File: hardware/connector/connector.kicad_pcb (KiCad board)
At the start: 2 copper layers, 60 x 40 mm, 4 parts

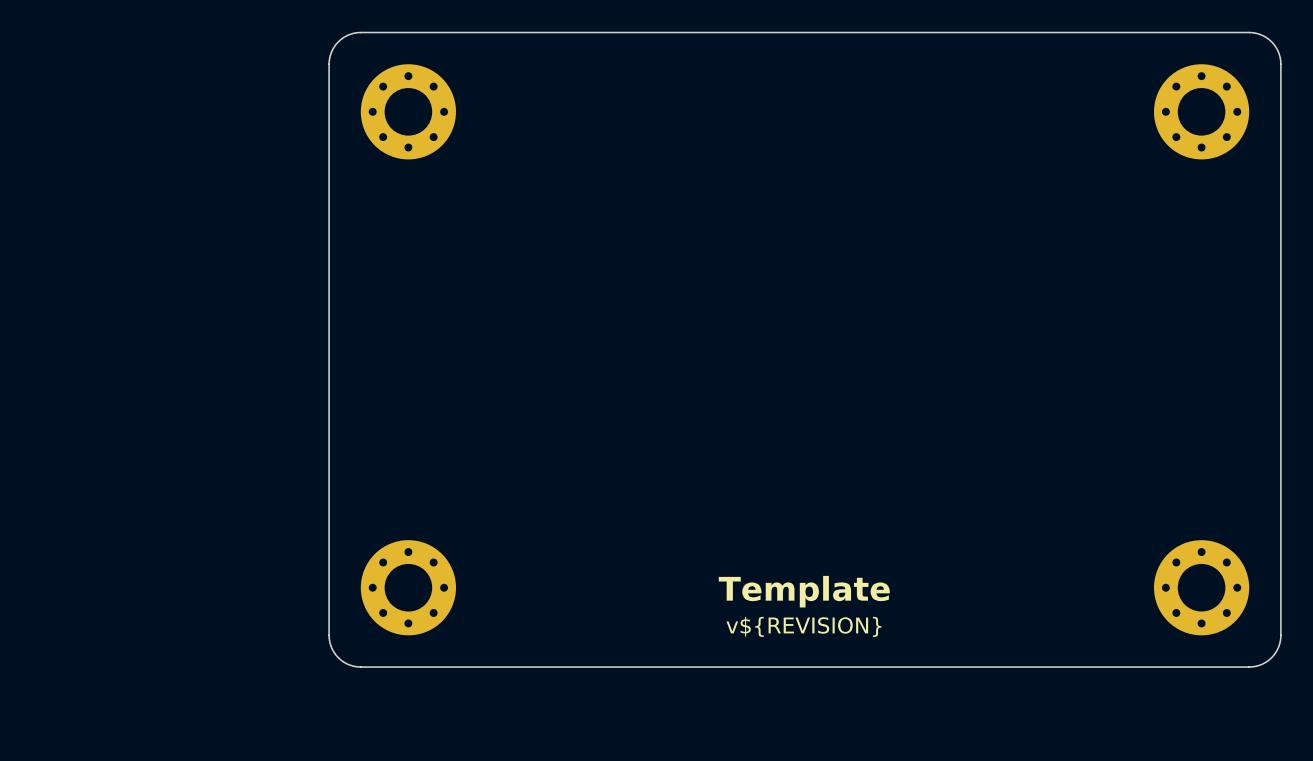
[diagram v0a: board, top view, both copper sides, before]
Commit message: Route PCB tracks
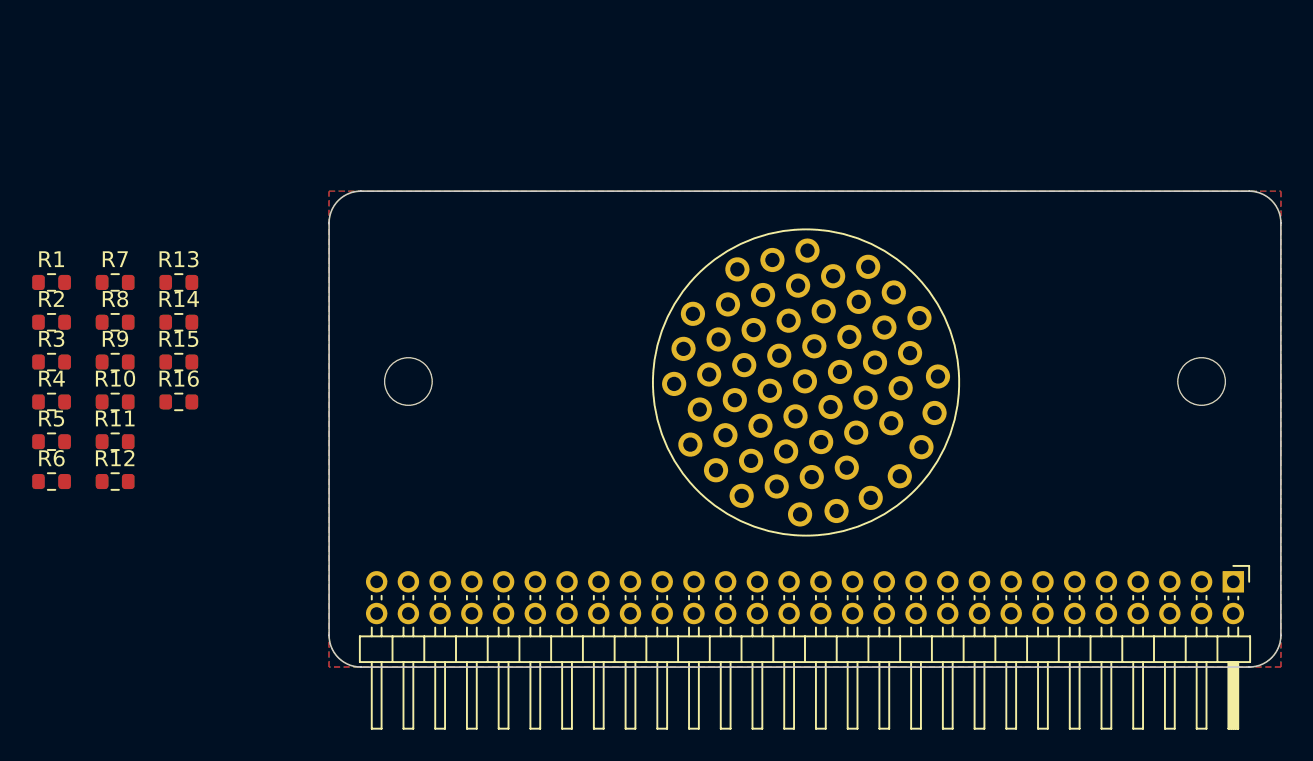
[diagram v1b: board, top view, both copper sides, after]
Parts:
- removed the REF** at (171.0, 81.0)
- removed the REF** at (121.0, 111.0)
- removed the REF** at (121.0, 81.0)
- removed the REF** at (171.0, 111.0)
- added J2: Autosport, Local_Library:AS022-55SN, B.Cu at (145.3, 98.6)
- added J3: Goldpin, Connector_PinHeader_2.00mm:PinHeader_2x28_P2.00mm_Horizontal, F.Cu at (173.0, 110.6)
- added R1: 0R, Resistor_SMD:R_0603_1608Metric, F.Cu at (98.5, 91.8)
- added R10: 0R, Resistor_SMD:R_0603_1608Metric, F.Cu at (102.5, 99.3)
- added R11: 0R, Resistor_SMD:R_0603_1608Metric, F.Cu at (102.5, 101.8)
- added R12: 0R, Resistor_SMD:R_0603_1608Metric, F.Cu at (102.5, 104.3)
- added R13: 0R, Resistor_SMD:R_0603_1608Metric, F.Cu at (106.5, 91.8)
- added R14: 0R, Resistor_SMD:R_0603_1608Metric, F.Cu at (106.5, 94.3)
- added R15: 0R, Resistor_SMD:R_0603_1608Metric, F.Cu at (106.5, 96.8)
- added R16: 0R, Resistor_SMD:R_0603_1608Metric, F.Cu at (106.5, 99.3)
- added R2: 0R, Resistor_SMD:R_0603_1608Metric, F.Cu at (98.5, 94.3)
- added R3: 0R, Resistor_SMD:R_0603_1608Metric, F.Cu at (98.5, 96.8)
- added R4: 0R, Resistor_SMD:R_0603_1608Metric, F.Cu at (98.5, 99.3)
- added R5: 0R, Resistor_SMD:R_0603_1608Metric, F.Cu at (98.5, 101.8)
- added R6: 0R, Resistor_SMD:R_0603_1608Metric, F.Cu at (98.5, 104.3)
- added R7: 0R, Resistor_SMD:R_0603_1608Metric, F.Cu at (102.5, 91.8)
- added R8: 0R, Resistor_SMD:R_0603_1608Metric, F.Cu at (102.5, 94.3)
- added R9: 0R, Resistor_SMD:R_0603_1608Metric, F.Cu at (102.5, 96.8)
- added REF**: MountingHole_3mm, MountingHole:MountingHole_3mm, F.Cu at (121.0, 98.0)
- added REF**: MountingHole_3mm, MountingHole:MountingHole_3mm, F.Cu at (171.0, 98.0)
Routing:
- added copper zone on B.Cu, net GND
- added copper zone on F.Cu, net GND
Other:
- board size 60 x 40 mm -> 60 x 30 mm
- board text removed: "Template"
- board text removed: "v${REVISION}"

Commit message: Route the tracks on the connector PCB
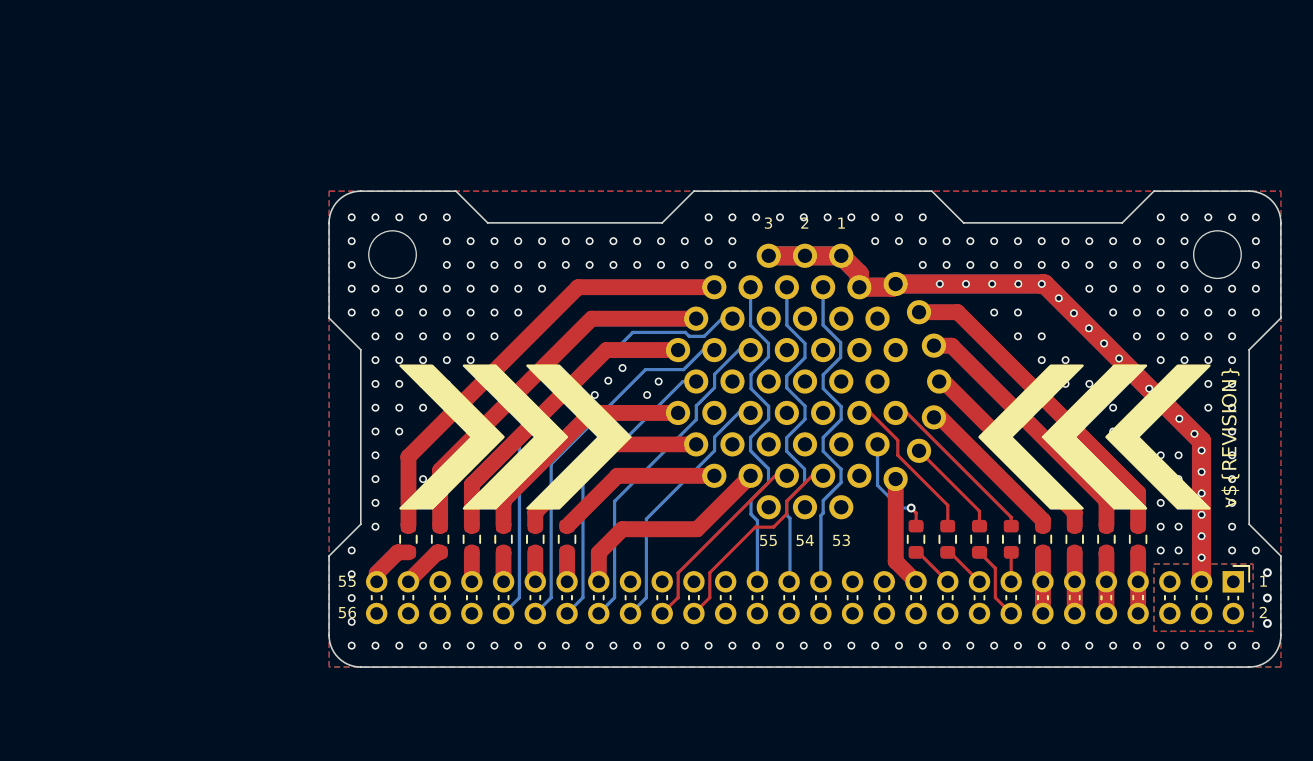
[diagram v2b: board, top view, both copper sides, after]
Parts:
- removed J3: Goldpin, Connector_PinHeader_2.00mm:PinHeader_2x28_P2.00mm_Horizontal
- removed R15, R16: 0R, Resistor_SMD:R_0603_1608Metric
- added J1: Conn_02x28_Top_Bottom, Local_Library:PinHeader_2x28_P2.00mm_Horizontal, F.Cu at (173.0, 110.6)
- J2: value Autosport -> D38999; footprint Local_Library:AS022-55SN -> Local_Library:DTS20W17-35SN
- moved R2 69.8 mm to (167.0, 107.9), turned to -90 degrees
- moved R4 67.1 mm to (165.0, 107.9), turned to -90 degrees
- moved R6 64.6 mm to (163.0, 107.9), turned to -90 degrees
- moved R7 60.7 mm to (161.0, 107.9), turned to -90 degrees
- moved R8 58.1 mm to (159.0, 107.9), turned to 90 degrees
- moved R11 54.8 mm to (157.0, 107.9), turned to 90 degrees
- moved R9 53.7 mm to (155.0, 107.9), turned to 90 degrees
- moved R12 50.6 mm to (153.0, 107.9), turned to 90 degrees
- moved R14 28.0 mm to (131.0, 107.9), turned to -90 degrees
- moved R1 27.7 mm to (121.0, 107.9), turned to 90 degrees
- moved R13 27.7 mm to (129.0, 107.9), turned to -90 degrees
- moved R5 27.2 mm to (125.0, 107.9), turned to 90 degrees
- moved R3 26.9 mm to (123.0, 107.9), turned to 90 degrees
- moved R10 26.0 mm to (127.0, 107.9), turned to -90 degrees
- moved REF** 8.06 mm to (120.0, 90.0)
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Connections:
- J2 pad 11: +5V_EXT -> SAFETY_IN_INV
- J2 pad 12: WATER_PRESSURE_IN1 -> SAFETY_IN_RES
- J2 pad 13: WATER_PRESSURE_IN2 -> SAFETY_IN_AS_TS_ON
- J2 pad 14: WATER_TEMPERATURE_IN1 -> SAFETY_IN_WHEEL_FL
- J2 pad 15: WATER_TEMPERATURE_IN2 -> LOAD_CELL_IN_L+
- J2 pad 16: MONO_TEMPERATURE_IN -> Net-(J2-Pin_16)
- J2 pad 17: POTENTIOMETER_IN_L -> Net-(J2-Pin_17)
- J2 pad 18: POTENTIOMETER_IN_R -> SAFETY_IN_HVD
- J2 pad 19: Net-(J2-Pin_19) -> SAFETY_IN_HV
- J2 pad 20: Net-(J2-Pin_20) -> SAFETY_IN_ASMS
- J2 pad 21: +3V_EXT -> SAFETY_IN_RFU
- J2 pad 22: LOAD_CELL_IN_L+ -> LOAD_CELL_IN_R-
- J2 pad 24: LOAD_CELL_IN_R+ -> Net-(J2-Pin_24)
- J2 pad 25: LOAD_CELL_IN_R- -> Net-(J2-Pin_25)
- J2 pad 26: Net-(J2-Pin_26) -> POTENTIOMETER_IN_R
- J2 pad 27: Net-(J2-Pin_27) -> POTENTIOMETER_IN_L
- J2 pad 28: Net-(J2-Pin_28) -> GND
- J2 pad 29: Net-(J2-Pin_29) -> WATER_TEMPERATURE_IN1
- J2 pad 30: Net-(J2-Pin_30) -> OIL_TEMPERATURE_RR
- J2 pad 31: Net-(J2-Pin_31) -> LOAD_CELL_IN_R+
- J2 pad 33: unconnected-(J2-Pin_33-Pad33) -> Net-(J2-Pin_33)
- J2 pad 34: unconnected-(J2-Pin_34-Pad34) -> Net-(J2-Pin_34)
- J2 pad 35: unconnected-(J2-Pin_35-Pad35) -> GND
- J2 pad 36: SAFETY_IN_INV -> GND
- J2 pad 37: SAFETY_IN_HVD -> SAFETY_IN_WHEEL_RR
- J2 pad 38: SAFETY_IN_RES -> MONO_TEMPERATURE_IN
- J2 pad 39: SAFETY_IN_HV -> Net-(J2-Pin_39)
- J2 pad 4: unconnected-(J2-Pin_4-Pad4) -> +24V
- J2 pad 40: SAFETY_IN_FW -> Net-(J2-Pin_40)
- J2 pad 41: SAFETY_IN_ASMS -> Net-(J2-Pin_41)
- J2 pad 42: SAFETY_IN_RFU1 -> GND
- J2 pad 43: SAFETY_IN_RFU2 -> GND
- J2 pad 44: SAFETY_IN_WHEEL_FL -> GND
- J2 pad 45: SAFETY_IN_WHEEL_FR -> OIL_TEMPERATURE_RL
- J2 pad 46: SAFETY_IN_WHEEL_RL -> Net-(J2-Pin_46)
- J2 pad 47: SAFETY_IN_WHEEL_RR -> +5V_EXT
- J2 pad 48: Net-(J2-Pin_48) -> SAFETY_IN_FW
- J2 pad 49: Net-(J2-Pin_49) -> SAFETY_IN_WHEEL_FR
- J2 pad 5: unconnected-(J2-Pin_5-Pad5) -> +24V
- J2 pad 50: Net-(J2-Pin_50) -> SAFETY_IN_WHEEL_RL
- J2 pad 51: unconnected-(J2-Pin_51-Pad51) -> +3V_EXT
- J2 pad 52: unconnected-(J2-Pin_52-Pad52) -> Net-(J2-Pin_52)
- J2 pad 6: unconnected-(J2-Pin_6-Pad6) -> WATER_PRESSURE_IN1
- J2 pad 7: Net-(J2-Pin_7) -> WATER_PRESSURE_IN2
- J2 pad 8: Net-(J2-Pin_8) -> WATER_TEMPERATURE_IN2
- R1 pad 1: CAN+ -> RTDS_OUT
- R1 pad 2: Net-(J2-Pin_7) -> Net-(J2-Pin_9)
- R10 pad 1: Net-(J2-Pin_29) -> Net-(J2-Pin_39)
- R10 pad 2: FAN_OUT_L -> ASSI_OUT_B
- R11 pad 1: Net-(J2-Pin_30) -> CAN-
- R11 pad 2: FAN_OUT_R -> Net-(J2-Pin_40)
- R12 pad 1: Net-(J2-Pin_31) -> CAN2-
- R12 pad 2: PUMP_OUT1 -> Net-(J2-Pin_41)
- R13 pad 1: Net-(J2-Pin_32) -> Net-(J2-Pin_46)
- R13 pad 2: PUMP_OUT2 -> ASSI_OUT_G
- R14 pad 1: Net-(J2-Pin_48) -> Net-(J2-Pin_52)
- R2 pad 1: CAN- -> Net-(J2-Pin_10)
- R2 pad 2: Net-(J2-Pin_8) -> PUMP_OUT1
- R3 pad 1: CAN2+ -> ASSI_OUT_BUZZER
- R3 pad 2: Net-(J2-Pin_9) -> Net-(J2-Pin_16)
- R4 pad 1: CAN2- -> Net-(J2-Pin_17)
- R4 pad 2: Net-(J2-Pin_10) -> PUMP_OUT2
- R5 pad 1: ANALOG_IN_RFU1 -> BRAKE_LIGHT_OUT
- R5 pad 2: Net-(J2-Pin_19) -> Net-(J2-Pin_24)
- R6 pad 1: ANALOG_IN_RFU2 -> Net-(J2-Pin_25)
- R6 pad 2: Net-(J2-Pin_20) -> FAN_OUT_L
- R7 pad 1: BRAKE_LIGHT_OUT -> Net-(J2-Pin_32)
- R7 pad 2: Net-(J2-Pin_26) -> FAN_OUT_R
- R8 pad 1: ASSI_OUT_BUZZER -> CAN+
- R8 pad 2: Net-(J2-Pin_27) -> Net-(J2-Pin_33)
- R9 pad 1: RTDS_OUT -> CAN2+
- R9 pad 2: Net-(J2-Pin_28) -> Net-(J2-Pin_34)
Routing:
- net +24V: track 0.00 -> 125.0 mm, vias 0 -> 21
- net Net-(J2-Pin_9): track 0.00 -> 28.1 mm
- net LOAD_CELL_IN_L+: track 0.00 -> 27.9 mm
- net LOAD_CELL_IN_L-: track 0.00 -> 23.8 mm
- net Net-(J2-Pin_16): track 0.00 -> 23.6 mm
- net SAFETY_IN_RES: track 0.00 -> 22.9 mm
- net SAFETY_IN_INV: track 0.00 -> 22.7 mm
- net SAFETY_IN_AS_TS_ON: track 0.00 -> 21.9 mm
- net LOAD_CELL_IN_R-: track 0.00 -> 21.7 mm
- net WATER_TEMPERATURE_IN2: track 0.00 -> 21.5 mm
- net WATER_PRESSURE_IN2: track 0.00 -> 21.5 mm
- net WATER_PRESSURE_IN1: track 0.00 -> 21.4 mm
- net SAFETY_IN_WHEEL_FL: track 0.00 -> 21.1 mm
- net SAFETY_IN_ASMS: track 0.00 -> 20.8 mm
- net Net-(J2-Pin_10): track 0.00 -> 20.6 mm
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- added copper zone on B.Cu, net +24V
- added copper zone on F.Cu, net +24V
- added copper zone on In1.Cu, net +24V
- added copper zone on In1.Cu, net GND
- added copper zone on In2.Cu, net GND
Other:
- outline, holes or cut-outs redrawn
- copper layers 2 -> 4
- board text added: "1"
- board text added: "2"
- board text added: "3"
- board text added: "53"
- board text added: "54"
- board text added: "55"
- board text added: "56"
- board text added: "JLCJLCJLCJLC"
- board text added: "v${REVISION}"

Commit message: Fix connector wiring
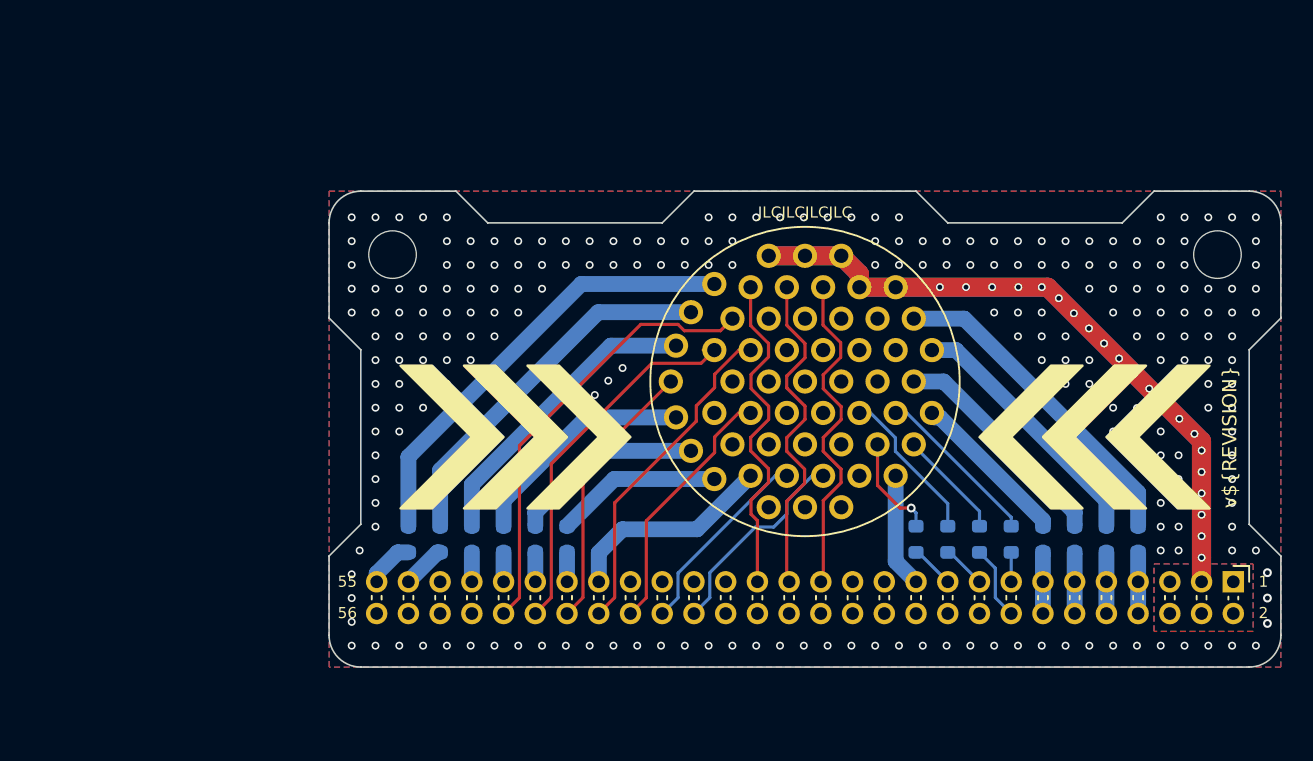
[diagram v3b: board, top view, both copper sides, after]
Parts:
- J2: moved to F.Cu
- R1, R12, R14, R6: moved to B.Cu
- R10: renamed from R7; moved to B.Cu
- R11: renamed from R13; moved to B.Cu
- R13: renamed from R11; moved to B.Cu
- R2: renamed from R3; moved to B.Cu
- R3: renamed from R2; moved to B.Cu
- R4: renamed from R5; moved to B.Cu
- R5: renamed from R4; moved to B.Cu
- R7: renamed from R10; moved to B.Cu
- R8: renamed from R9; moved to B.Cu
- R9: renamed from R8; moved to B.Cu
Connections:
- J2 pad 11: SAFETY_IN_INV -> LOAD_CELL_IN_L+
- J2 pad 12: SAFETY_IN_RES -> SAFETY_IN_WHEEL_FL
- J2 pad 14: SAFETY_IN_WHEEL_FL -> SAFETY_IN_RES
- J2 pad 15: LOAD_CELL_IN_L+ -> SAFETY_IN_INV
- J2 pad 18: SAFETY_IN_HVD -> LOAD_CELL_IN_L-
- J2 pad 19: SAFETY_IN_HV -> LOAD_CELL_IN_R-
- J2 pad 20: SAFETY_IN_ASMS -> SAFETY_IN_RFU
- J2 pad 21: SAFETY_IN_RFU -> SAFETY_IN_ASMS
- J2 pad 22: LOAD_CELL_IN_R- -> SAFETY_IN_HV
- J2 pad 23: LOAD_CELL_IN_L- -> SAFETY_IN_HVD
- J2 pad 25: Net-(J2-Pin_25) -> LOAD_CELL_IN_R+
- J2 pad 26: POTENTIOMETER_IN_R -> OIL_TEMPERATURE_RR
- J2 pad 27: POTENTIOMETER_IN_L -> WATER_TEMPERATURE_IN1
- J2 pad 29: WATER_TEMPERATURE_IN1 -> POTENTIOMETER_IN_L
- J2 pad 30: OIL_TEMPERATURE_RR -> POTENTIOMETER_IN_R
- J2 pad 31: LOAD_CELL_IN_R+ -> Net-(J2-Pin_31)
- J2 pad 33: Net-(J2-Pin_33) -> MONO_TEMPERATURE_IN
- J2 pad 34: Net-(J2-Pin_34) -> SAFETY_IN_WHEEL_RR
- J2 pad 37: SAFETY_IN_WHEEL_RR -> Net-(J2-Pin_37)
- J2 pad 38: MONO_TEMPERATURE_IN -> Net-(J2-Pin_38)
- J2 pad 4: +24V -> Net-(J2-Pin_4)
- J2 pad 41: Net-(J2-Pin_41) -> OIL_TEMPERATURE_RL
- J2 pad 45: OIL_TEMPERATURE_RL -> Net-(J2-Pin_45)
- J2 pad 47: +5V_EXT -> Net-(J2-Pin_47)
- J2 pad 48: SAFETY_IN_FW -> +3V_EXT
- J2 pad 49: SAFETY_IN_WHEEL_FR -> SAFETY_IN_WHEEL_RL
- J2 pad 5: +24V -> WATER_TEMPERATURE_IN2
- J2 pad 50: SAFETY_IN_WHEEL_RL -> SAFETY_IN_WHEEL_FR
- J2 pad 51: +3V_EXT -> SAFETY_IN_FW
- J2 pad 52: Net-(J2-Pin_52) -> +5V_EXT
- J2 pad 6: WATER_PRESSURE_IN1 -> WATER_PRESSURE_IN2
- J2 pad 7: WATER_PRESSURE_IN2 -> WATER_PRESSURE_IN1
- J2 pad 8: WATER_TEMPERATURE_IN2 -> +24V
- J2 pad 9: Net-(J2-Pin_9) -> +24V
- R1 pad 2: Net-(J2-Pin_9) -> Net-(J2-Pin_4)
- R10 pad 1: Net-(J2-Pin_32) -> Net-(J2-Pin_39)
- R11 pad 1: Net-(J2-Pin_46) -> Net-(J2-Pin_40)
- R12 pad 2: Net-(J2-Pin_41) -> Net-(J2-Pin_45)
- R13 pad 2: Net-(J2-Pin_40) -> Net-(J2-Pin_46)
- R14 pad 1: Net-(J2-Pin_52) -> Net-(J2-Pin_47)
- R2 pad 2: Net-(J2-Pin_16) -> Net-(J2-Pin_10)
- R3 pad 1: Net-(J2-Pin_10) -> Net-(J2-Pin_16)
- R4 pad 2: Net-(J2-Pin_24) -> Net-(J2-Pin_17)
- R5 pad 1: Net-(J2-Pin_17) -> Net-(J2-Pin_24)
- R6 pad 1: Net-(J2-Pin_25) -> Net-(J2-Pin_31)
- R7 pad 1: Net-(J2-Pin_39) -> Net-(J2-Pin_32)
- R8 pad 2: Net-(J2-Pin_34) -> Net-(J2-Pin_37)
- R9 pad 2: Net-(J2-Pin_33) -> Net-(J2-Pin_38)
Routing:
- net Net-(J2-Pin_4): track 0.00 -> 28.2 mm
- net Net-(J2-Pin_9): track 28.1 -> 0.00 mm
- net Net-(J2-Pin_31): track 0.00 -> 14.4 mm
- net Net-(J2-Pin_25): track 12.8 -> 0.00 mm
- net Net-(J2-Pin_52): track 10.6 -> 0.00 mm
- net Net-(J2-Pin_38): track 0.00 -> 10.6 mm
- net Net-(J2-Pin_33): track 10.6 -> 0.00 mm
- net Net-(J2-Pin_47): track 0.00 -> 10.5 mm
- net Net-(J2-Pin_37): track 0.00 -> 9.86 mm
- net Net-(J2-Pin_34): track 9.86 -> 0.00 mm
- net Net-(J2-Pin_45): track 0.00 -> 6.57 mm, vias 0 -> 1
- net Net-(J2-Pin_41): track 6.57 -> 0.00 mm, vias 1 -> 0
- net Net-(J2-Pin_46): track 12.8 -> 6.33 mm
- net Net-(J2-Pin_40): track 6.33 -> 12.2 mm
- net Net-(J2-Pin_39): track 14.9 -> 9.93 mm
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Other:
- outline, holes or cut-outs redrawn
- board text added: "25"
